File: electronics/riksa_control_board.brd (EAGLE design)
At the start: 50 x 65 mm, 50 parts

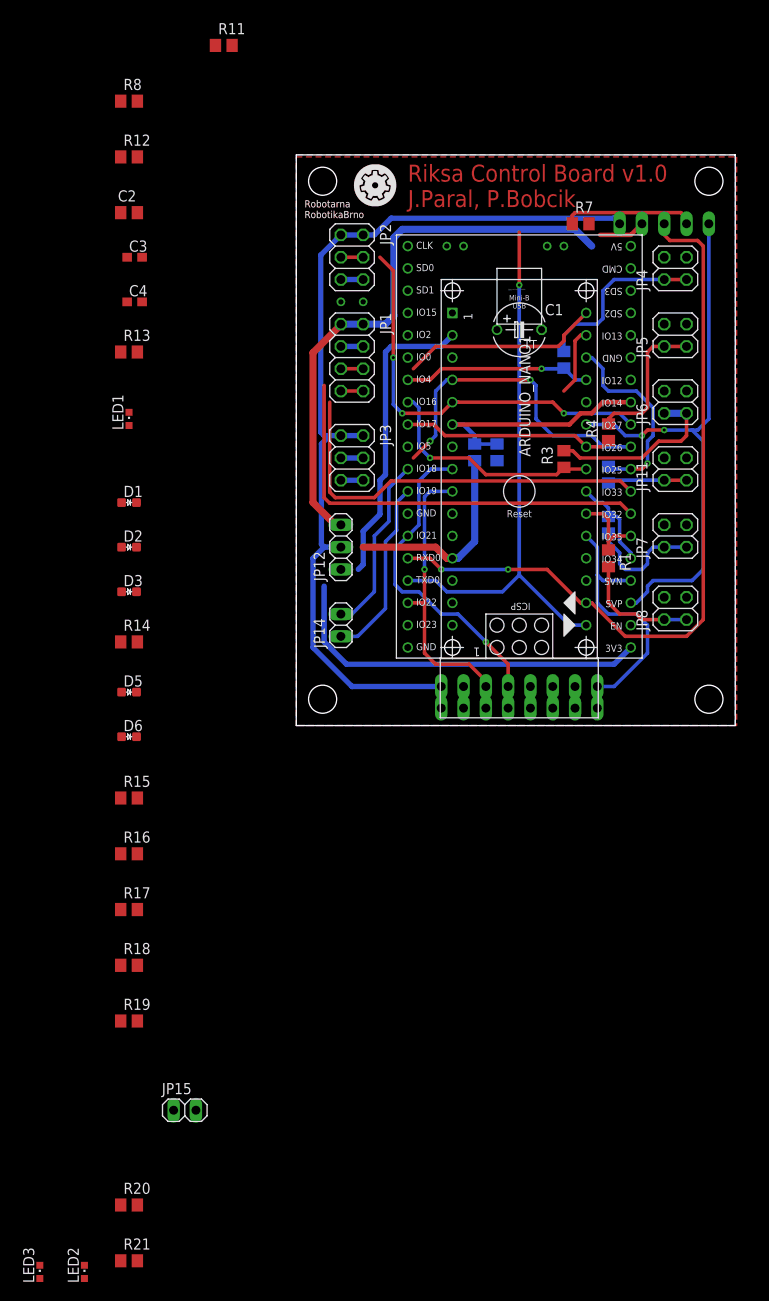
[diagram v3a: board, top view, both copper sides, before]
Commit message: ELE: new layout of board from @PetrBobcik - apply changes in schema from @cednik
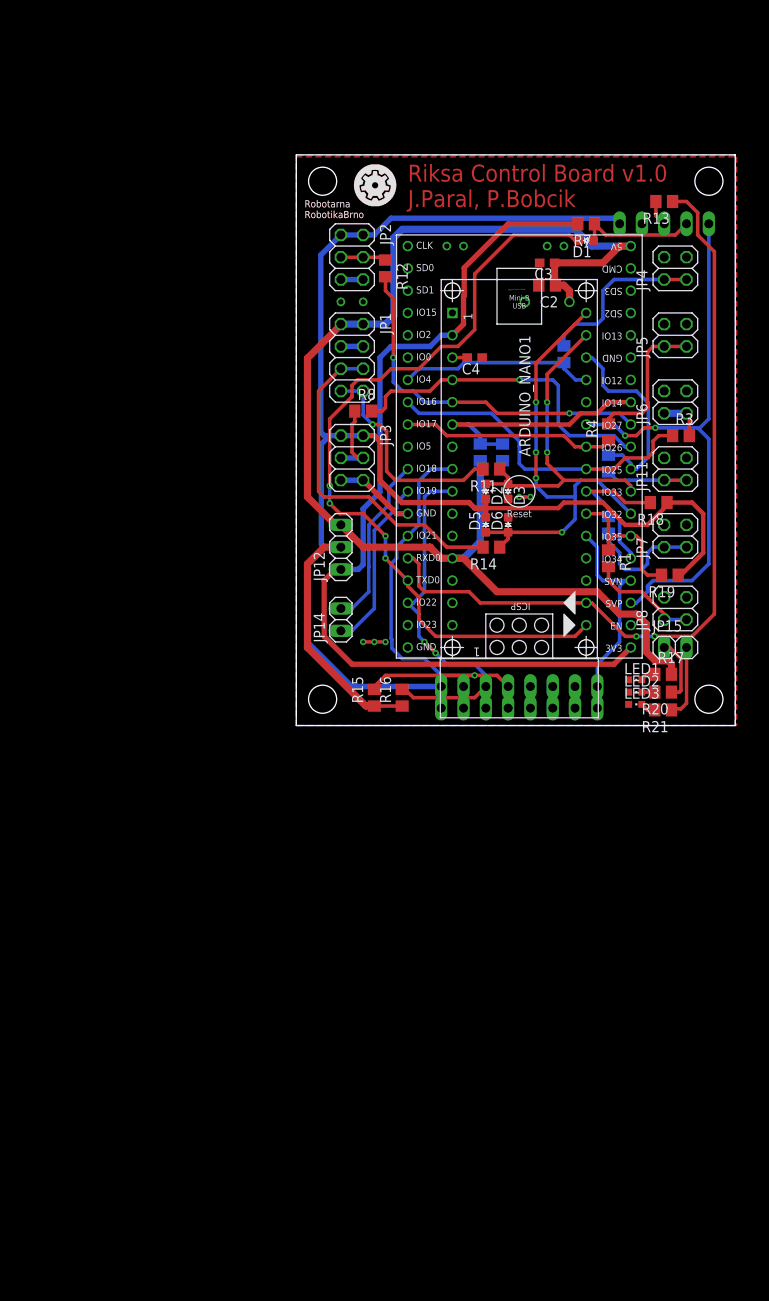
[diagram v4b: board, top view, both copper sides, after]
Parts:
- moved LED3 93.7 mm to (38.6, 2.41), turned to 270 degrees
- moved LED2 91.1 mm to (38.6, 3.81), turned to 270 degrees
- moved R21 87.4 mm to (41.8, 1.78), turned to 180 degrees
- moved R20 84.3 mm to (41.8, 3.81), turned to 180 degrees
- moved R18 80.1 mm to (41.3, 25.4), turned to 180 degrees
- moved R19 79.8 mm to (42.5, 17.1), turned to 180 degrees
- moved JP15 76.8 mm to (43.2, 8.89)
- moved R17 66.5 mm to (41.8, 5.84)
- moved LED1 64.9 mm to (38.6, 5.21), turned to 270 degrees
- moved R13 63.3 mm to (41.9, 59.7), turned to 180 degrees
- moved D1 60.0 mm to (33.0, 55.2), turned to 180 degrees
- moved R11 57.1 mm to (22.2, 29.2), turned to 180 degrees
- moved D6 49.5 mm to (24.1, 22.9), turned to 90 degrees
- moved C2 48.3 mm to (28.6, 50.2), turned to 180 degrees
- moved C3 47.0 mm to (28.6, 52.7), turned to 180 degrees
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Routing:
- net VCC: track 107.2 -> 193.7 mm
- net +5V: track 87.7 -> 145.5 mm
- net D12_ROBOCLAW_TX_: track 2.54 -> 39.2 mm
- net +3V3: track 77.6 -> 105.5 mm
- net TX->: track 63.1 -> 90.7 mm, vias 1 -> 4
- net D11_ROBOCLAW_RX_: track 2.54 -> 25.9 mm, vias 0 -> 1
- net D12_ROBOCLAW_TX: track 71.1 -> 51.9 mm, vias 0 -> 4
- net MPU_SDA: track 38.9 -> 54.6 mm
- net D5_LED_FORWADR_: track 20.4 -> 5.21 mm
- net D11_ROBOCLAW_RX: track 53.8 -> 39.0 mm, vias 0 -> 2
- net MPU_SCL: track 34.5 -> 45.3 mm, vias 1 -> 2
- net D5_LED_FORWADR: track 26.8 -> 37.1 mm, vias 1 -> 0
- net D4_BTN_REVERSE: track 10.7 -> 19.1 mm
- net LED_YELLOW: track 0.00 -> 8.38 mm
- net LED_RED: track 0.00 -> 7.22 mm
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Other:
- board text added: "B_ST"
- board text added: "LED"
- board text removed: "B_STOP"

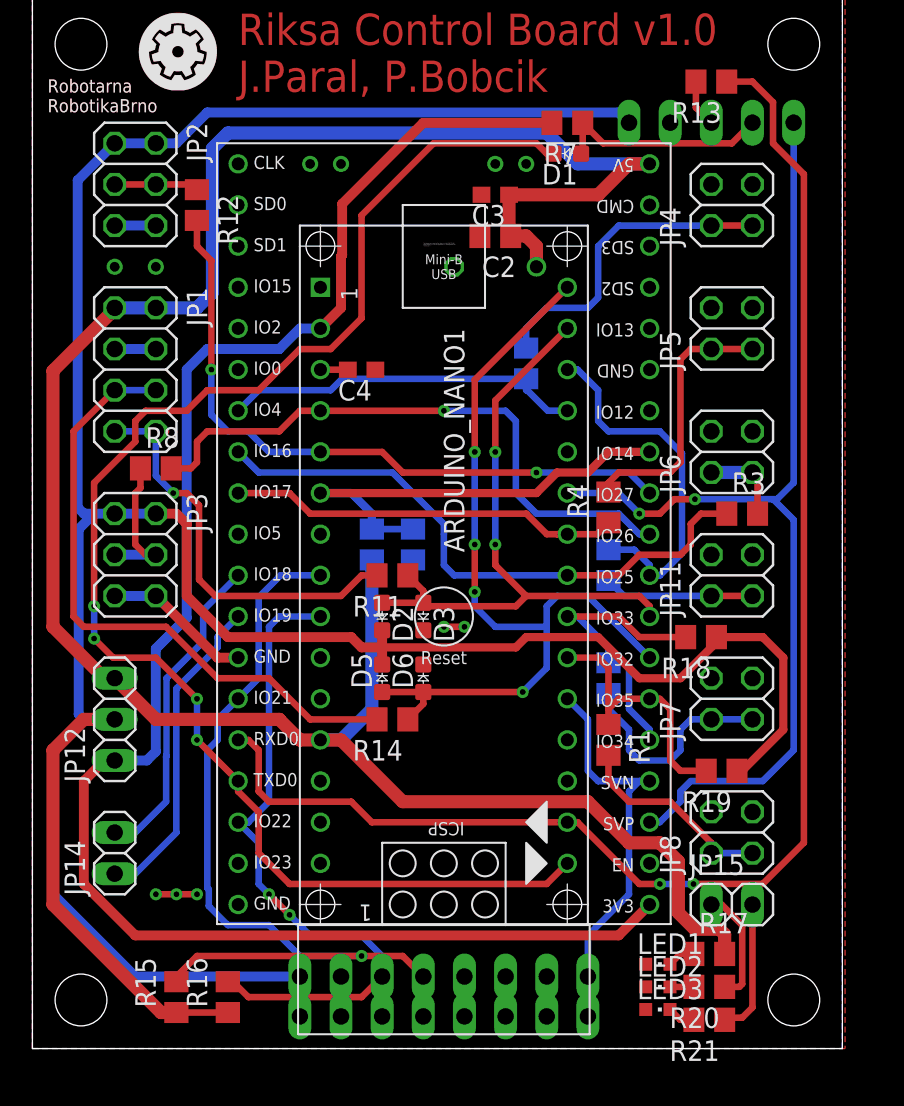
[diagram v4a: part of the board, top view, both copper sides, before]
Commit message: ELE: some improves in layout by @PetrBobcik
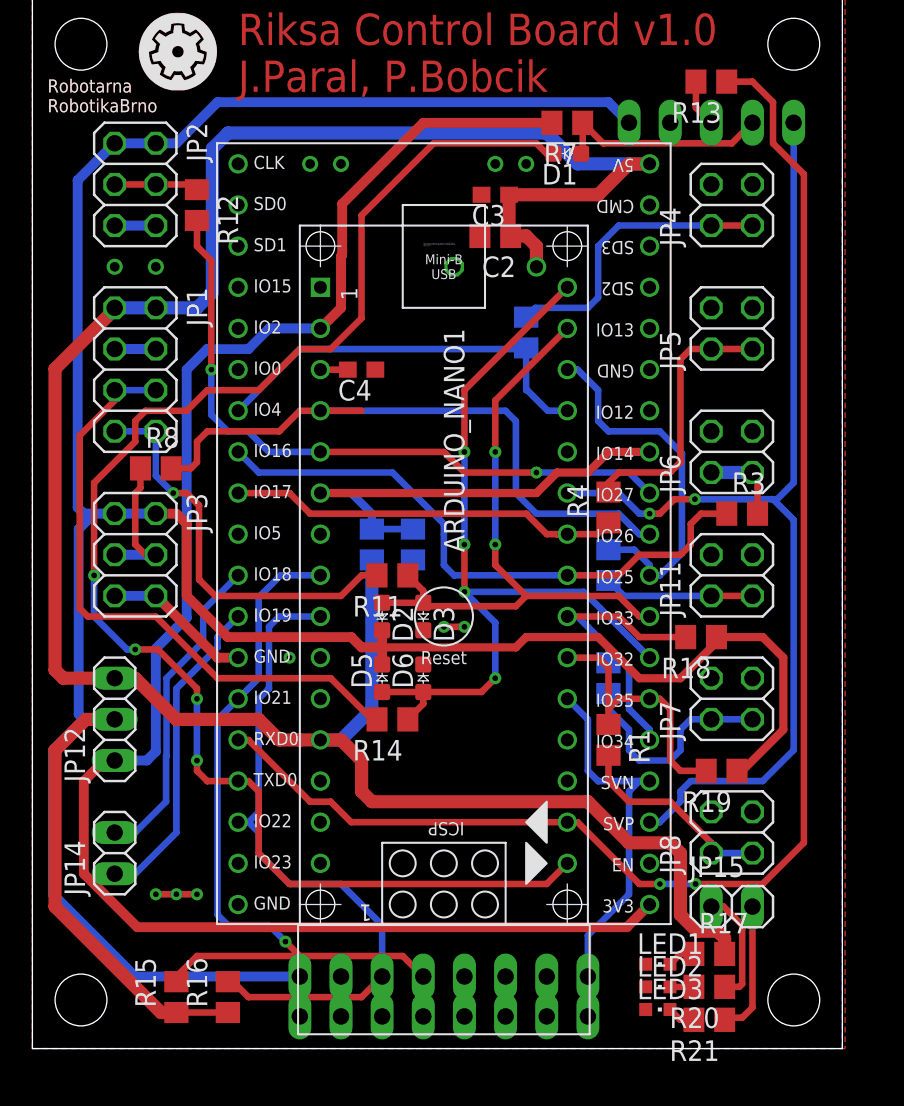
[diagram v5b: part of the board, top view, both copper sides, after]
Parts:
- moved R5 1.91 mm to (30.5, 44.2)
- moved JP15 0.13 mm to (43.2, 8.76)
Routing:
- net MPU_SDA: track 54.6 -> 50.2 mm
- net +5V: track 145.5 -> 148.2 mm
- net D9_LED_STOP: track 22.4 -> 25.1 mm
- net A0_POT_LEFT: track 37.5 -> 40.1 mm, vias 1 -> 0
- net D12_ROBOCLAW_TX: track 51.9 -> 50.1 mm
- net D9_LED_STOP_: track 19.7 -> 18.2 mm
- net RX<-: track 91.0 -> 89.6 mm
- net TX->: track 90.7 -> 91.8 mm
- net D12_ROBOCLAW_TX_: track 39.2 -> 38.4 mm
- net +3V3: track 105.5 -> 104.7 mm
- net MPU_SCL: track 45.3 -> 45.0 mm, vias 2 -> 0
- net GND: vias 11 -> 12

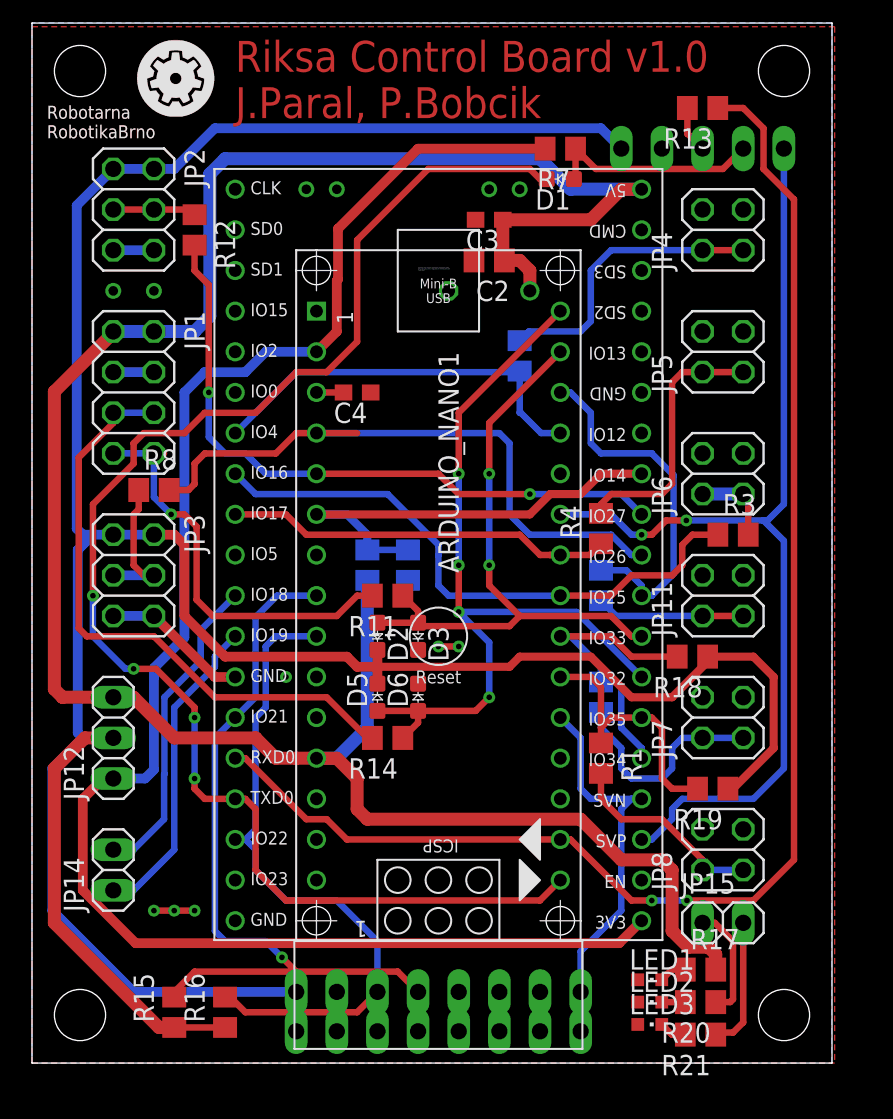
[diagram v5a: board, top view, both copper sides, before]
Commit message: ELE: some improves in layout and schema by @PetrBobcik
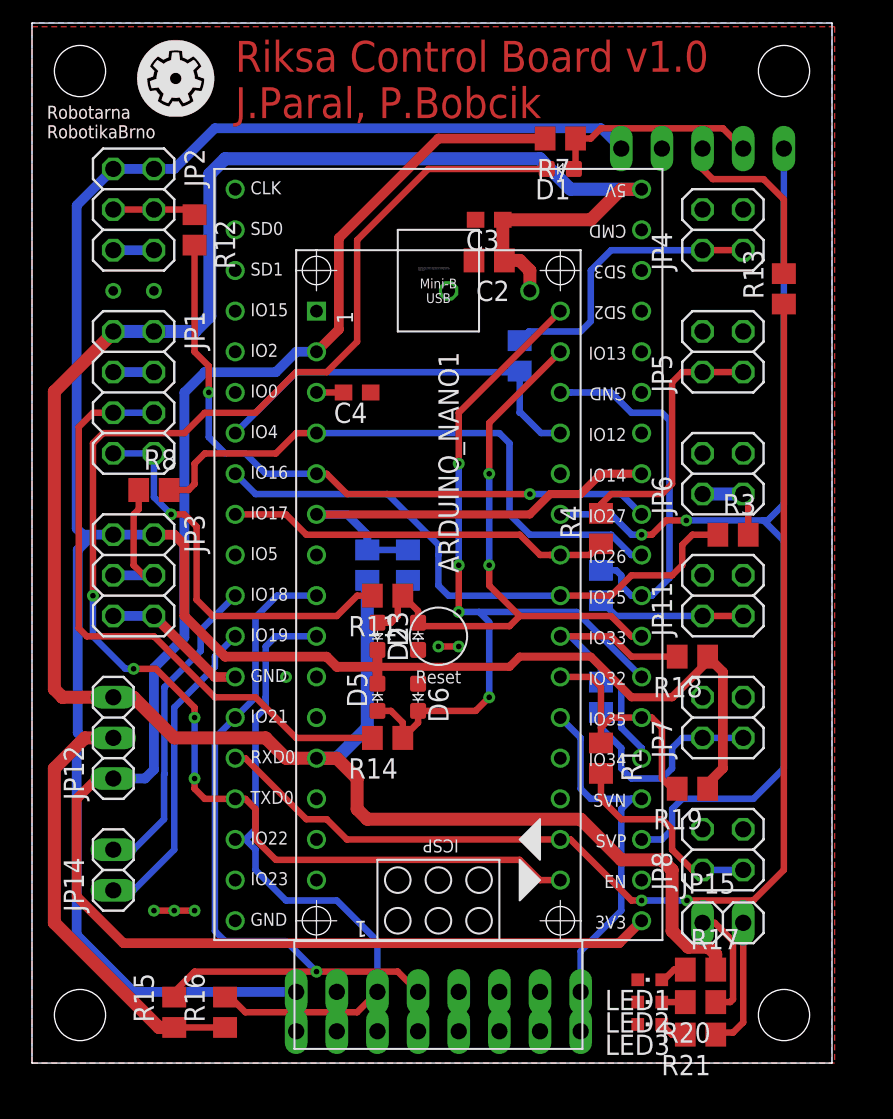
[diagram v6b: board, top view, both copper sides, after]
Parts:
- moved R13 12.4 mm to (47.0, 48.4), turned to 90 degrees
- moved R19 1.27 mm to (41.3, 17.1)
- moved D1 0.64 mm to (33.0, 55.9)
- moved R7 0.63 mm to (33.0, 57.8)
- turned D3 to 90 degrees
- turned D6 to 270 degrees
- turned LED1 to 90 degrees
- turned LED2 to 90 degrees
- turned LED3 to 90 degrees
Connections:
- removed net LED_GREEN_: LED1.C, R17.1
- removed net LED_RED_: LED2.C, R20.2
- removed net LED_YELLOW_: LED3.C, R21.2
- new net N$11: LED1.A, R17.1
- new net N$2: LED3.A, R21.2
- new net N$8: LED2.A, R20.2
- net D11_ROBOCLAW_RX: now also D3.C; no longer D3.A
- net D12_ROBOCLAW_TX: now also D6.C; no longer D6.A
- net GND: now also D3.A, D6.A, LED1.C, LED2.C, LED3.C; no longer D3.C, D6.C, LED1.A, LED2.A, LED3.A
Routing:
- net RX<-: track 89.6 -> 74.1 mm
- net RX<-_: track 2.97 -> 11.8 mm
- net VCC: track 194.1 -> 188.8 mm
- net A0_POT_LEFT: track 40.1 -> 37.5 mm
- net N$11: track 0.00 -> 1.74 mm
- net N$2: track 0.00 -> 1.74 mm
- net LED_YELLOW_: track 1.74 -> 0.00 mm
- net LED_GREEN_: track 1.74 -> 0.00 mm
- net N$8: track 0.00 -> 1.48 mm
- net LED_RED_: track 1.48 -> 0.00 mm
- net MPU_SDA: track 50.2 -> 51.5 mm
- net D3_BTN_STOP: track 16.3 -> 15.0 mm
- net TX->: track 91.8 -> 90.9 mm
- net +3V3: track 104.7 -> 105.6 mm
- net D12_ROBOCLAW_TX_: track 38.4 -> 39.2 mm
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
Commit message: ELE: final version of board
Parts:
- added C5: 470u/10V, rcl:TT5D6
- moved C3 6.38 mm to (34.9, 53.3), flipped to the bottom, turned to 270 degrees
- moved C2 4.96 mm to (32.4, 53.3), flipped to the bottom, turned to 270 degrees
- moved C1 3.24 mm to (25.4, 47.6)
- moved R17 1.79 mm to (40.0, 6.03), flipped to the bottom, turned to 180 degrees
- moved R21 1.79 mm to (40.0, 1.59), flipped to the bottom, turned to 0 degrees
- moved R20 1.78 mm to (40.0, 3.81), flipped to the bottom, turned to 0 degrees
- moved LED1 1.40 mm to (40.0, 5.08), turned to 270 degrees
- moved LED3 1.40 mm to (40.0, 2.54), turned to 270 degrees
- moved LED2 1.40 mm to (40.0, 3.81), turned to 270 degrees
- moved R8 1.31 mm to (6.35, 35.5)
- moved R13 0.63 mm to (47.6, 48.4), flipped to the bottom
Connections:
- net +5V: now also C5.+
- net GND: now also C5.-
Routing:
- net +5V: track 148.2 -> 124.6 mm, vias 0 -> 1
- net RX<-_: track 11.8 -> 16.1 mm
- net RX<-: track 74.1 -> 77.6 mm, vias 2 -> 1
- net A0_POT_LEFT: track 37.5 -> 38.9 mm
- net BT_STATE: track 65.0 -> 63.8 mm
- net VCC: track 188.8 -> 187.8 mm
- net LED_RED: track 7.17 -> 6.17 mm
- net LED_YELLOW: track 8.26 -> 9.06 mm
- net N$2: track 1.74 -> 2.50 mm, vias 0 -> 1
- net N$11: track 1.74 -> 2.50 mm, vias 0 -> 1
- net N$8: track 1.48 -> 2.11 mm, vias 0 -> 1
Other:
- board text added: "Riksa Control Board v1.0 J.Paral, P.Bobcik CC BY-SA 4.0"
